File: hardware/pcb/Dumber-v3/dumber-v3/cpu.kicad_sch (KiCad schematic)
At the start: 30 parts, among them J1 Conn_02x03_Odd_Even, J2 Conn_02x03_Odd_Even, J3 Conn_02x05_Odd_Even, M1 Motor, M2 Motor, Q2 PMN52XP, U1 XBEE-3, U2 STM32F071CBTx, U7 A3909

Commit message: Mise a jour PCB et coque. Des fichiers STEP ne sont pas encore remontés car trop gros
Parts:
- removed D3, D4, D5: LED, Diode_SMD:D_0805_2012Metric, symbol Device:LED
- removed R16, R22: 1K, Resistor_SMD:R_0805_2012Metric, symbol Device:R
- removed R23: 820, Resistor_SMD:R_0805_2012Metric, symbol Device:R
- added J4: TE 1-84982-0, INSA:TE 1-84982-0, symbol Connector_Generic:Conn_01x10
- added RN1, RN2: 1K, Resistor_SMD:R_Array_Convex_4x1206, symbol Device:R_Pack04
- J3: footprint Connector_PinHeader_1.27mm:PinHeader_2x05_P1.27mm_Vertical_SMD -> Connector_PinHeader_1.27mm:PinHeader_2x05_P1.27mm_Horizontal
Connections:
- net +2V5: now also U2.36 (VDDIO2)
- net GND: now also J4.1 (Pin_1)
- net SEG_D: now reaches U2.29 (PA8)
- net SEG_D: now also RN1.4 (R4.1)
- net SEG_E: now reaches U2.30 (PA9)
- net SEG_E: now also RN2.4 (R4.1)
- net SEG_F: now reaches U2.32 (PA11)
- net SEG_F: now also RN2.3 (R3.1)
- net SEG_G: now reaches U2.33 (PA12)
- net SEG_G: now also RN2.2 (R2.1)
- net SEG_DP: now reaches U2.38 (PA15)
- net SEG_DP: now also RN2.1 (R1.1)
- net LED_ORANGE renamed SEG_B
- net SEG_B: now also RN1.2 (R2.1)
- net LED_ROUGE renamed SEG_A
- net SEG_A: now also RN1.1 (R1.1)
- net LED_VERTE renamed SEG_C
- net SEG_C: now also RN1.3 (R3.1)
- new net: J4.6 (Pin_6), RN2.5 (R4.2)
- new net: J4.7 (Pin_7), RN2.6 (R3.2)
- new net: J4.8 (Pin_8), RN2.7 (R2.2)
- new net: J4.9 (Pin_9), RN2.8 (R1.2)
- new net: J4.5 (Pin_5), RN1.5 (R4.2)
- new net: J4.4 (Pin_4), RN1.6 (R3.2)
- new net: J4.3 (Pin_3), RN1.7 (R2.2)
- new net: J4.2 (Pin_2), RN1.8 (R1.2)
- new net BUTTON_PRESS: J4.10 (Pin_10)
- no-connect marks 16 -> 24

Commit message: Mise a jour sur les pcbs de dumber v3
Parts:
- removed RN1, RN2: 1K, Resistor_SMD:R_Array_Convex_4x1206, symbol Device:R_Pack04
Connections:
- net SEG_A: now also J4.2 (Pin_2)
- net SEG_B: now also J4.3 (Pin_3)
- net SEG_C: now also J4.4 (Pin_4)
- net SEG_D: now also J4.5 (Pin_5)
- net SEG_DP: now also J4.9 (Pin_9)
- net SEG_E: now also J4.6 (Pin_6)
- net SEG_F: now also J4.7 (Pin_7)
- net SEG_G: now also J4.8 (Pin_8)
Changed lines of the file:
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@@
     (stroke (width 0) (type default) (color 0 0 0 0))
   )
-  (wire (pts (xy 39.37 50.8) (xy 39.37 45.72))
+  (wire (pts (xy 39.37 45.72) (xy 39.37 69.85))
     (stroke (width 0) (type default) (color 0 0 0 0))
   )
@@
     (stroke (width 0) (type default) (color 0 0 0 0))
   )
-  (wire (pts (xy 34.29 60.96) (xy 34.29 80.01))
-    (stroke (width 0) (type default) (color 0 0 0 0))
-  )
-  (wire (pts (xy 52.07 50.8) (xy 52.07 45.72))
+  (wire (pts (xy 52.07 45.72) (xy 52.07 69.85))
     (stroke (width 0) (type default) (color 0 0 0 0))
   )
@@
     (stroke (width 0) (type default) (color 0 0 0 0))
   )
-  (wire (pts (xy 36.83 50.8) (xy 36.83 44.45))
+  (wire (pts (xy 36.83 44.45) (xy 36.83 69.85))
     (stroke (width 0) (type default) (color 0 0 0 0))
   )
@@
     (stroke (width 0) (type default) (color 0 0 0 0))
   )
-  (wire (pts (xy 54.61 39.37) (xy 54.61 50.8))
+  (wire (pts (xy 54.61 39.37) (xy 54.61 69.85))
     (stroke (width 0) (type default) (color 0 0 0 0))
   )
@@
     (stroke (width 0) (type default) (color 0 0 0 0))
   )
-  (wire (pts (xy 31.75 60.96) (xy 31.75 80.01))
-    (stroke (width 0) (type default) (color 0 0 0 0))
-  )
   (wire (pts (xy 240.03 99.06) (xy 240.03 101.6))
     (stroke (width 0) (type default) (color 0 0 0 0))
@@
     (stroke (width 0) (type default) (color 0 0 0 0))
   )
-  (wire (pts (xy 54.61 60.96) (xy 54.61 80.01))
-    (stroke (width 0) (type default) (color 0 0 0 0))
-  )
   (wire (pts (xy 201.93 33.02) (xy 201.93 35.56))
     (stroke (width 0) (type default) (color 0 0 0 0))
   )
-  (wire (pts (xy 59.69 60.96) (xy 59.69 80.01))
-    (stroke (width 0) (type default) (color 0 0 0 0))
-  )
   (wire (pts (xy 232.41 29.21) (xy 232.41 38.1))
     (stroke (width 0) (type default) (color 0 0 0 0))
@@
     (stroke (width 0) (type default) (color 0 0 0 0))
   )
-  (wire (pts (xy 34.29 50.8) (xy 34.29 43.18))
+  (wire (pts (xy 34.29 43.18) (xy 34.29 69.85))
     (stroke (width 0) (type default) (color 0 0 0 0))
   )
@@
     (stroke (width 0) (type default) (color 0 0 0 0))
   )
-  (wire (pts (xy 57.15 50.8) (xy 57.15 41.91))
+  (wire (pts (xy 57.15 41.91) (xy 57.15 69.85))
     (stroke (width 0) (type default) (color 0 0 0 0))
   )
@@
     (stroke (width 0) (type default) (color 0 0 0 0))
   )
-  (wire (pts (xy 31.75 50.8) (xy 31.75 41.91))
-    (stroke (width 0) (type default) (color 0 0 0 0))
-  )
-  (wire (pts (xy 57.15 60.96) (xy 57.15 80.01))
+  (wire (pts (xy 31.75 41.91) (xy 31.75 69.85))
     (stroke (width 0) (type default) (color 0 0 0 0))
   )
@@
     (stroke (width 0) (type default) (color 0 0 0 0))
   )
-  (wire (pts (xy 59.69 50.8) (xy 59.69 43.18))
+  (wire (pts (xy 59.69 43.18) (xy 59.69 69.85))
     (stroke (width 0) (type default) (color 0 0 0 0))
   )
@@
     (stroke (width 0) (type default) (color 0 0 0 0))
   )
-  (wire (pts (xy 52.07 60.96) (xy 52.07 80.01))
-    (stroke (width 0) (type default) (color 0 0 0 0))
-  )
   (wire (pts (xy 110.49 78.74) (xy 116.84 78.74))
     (stroke (width 0) (type default) (color 0 0 0 0))
@@
     (stroke (width 0) (type default) (color 0 0 0 0))
   )
-  (wire (pts (xy 36.83 60.96) (xy 36.83 80.01))
-    (stroke (width 0) (type default) (color 0 0 0 0))
-  )
   (wire (pts (xy 113.03 48.26) (xy 116.84 48.26))
     (stroke (width 0) (type default) (color 0 0 0 0))
@@
     (stroke (width 0) (type default) (color 0 0 0 0))
   )
-  (wire (pts (xy 39.37 60.96) (xy 39.37 80.01))
-    (stroke (width 0) (type default) (color 0 0 0 0))
-  )
   (label "ENCDROIT_B" (at 172.72 78.74 180)
     (effects (font (size 1.27 1.27)) (justify right bottom))
@@
     (effects (font (size 1.27 1.27)) (justify right bottom))
   )
-  (label "SEG_F" (at 57.15 80.01 90)
-    (effects (font (size 1.27 1.27)) (justify left bottom))
-  )
-  (label "SEG_A" (at 31.75 80.01 90)
+  (label "SEG_F" (at 57.15 69.85 90)
+    (effects (font (size 1.27 1.27)) (justify left bottom))
+  )
+  (label "SEG_A" (at 31.75 69.85 90)
     (effects (font (size 1.27 1.27)) (justify left bottom))
   )
@@
     (effects (font (size 1.27 1.27)) (justify right bottom))
   )
-  (label "SEG_G" (at 54.61 80.01 90)
+  (label "SEG_G" (at 54.61 69.85 90)
     (effects (font (size 1.27 1.27)) (justify left bottom))
   )
@@
     (effects (font (size 1.27 1.27)) (justify right bottom))
   )
-  (label "SEG_C" (at 36.83 80.01 90)
-    (effects (font (size 1.27 1.27)) (justify left bottom))
-  )
-  (label "SEG_DP" (at 52.07 80.01 90)
+  (label "SEG_C" (at 36.83 69.85 90)
+    (effects (font (size 1.27 1.27)) (justify left bottom))
+  )
+  (label "SEG_DP" (at 52.07 69.85 90)
     (effects (font (size 1.27 1.27)) (justify left bottom))
   )
@@
     (effects (font (size 1.27 1.27)) (justify right bottom))
   )
-  (label "SEG_E" (at 59.69 80.01 90)
+  (label "SEG_E" (at 59.69 69.85 90)
     (effects (font (size 1.27 1.27)) (justify left bottom))
   )
@@
     (effects (font (size 1.27 1.27)) (justify right bottom))
   )
-  (label "SEG_B" (at 34.29 80.01 90)
+  (label "SEG_B" (at 34.29 69.85 90)
     (effects (font (size 1.27 1.27)) (justify left bottom))
   )
@@
     (effects (font (size 1.27 1.27)) (justify right bottom))
   )
-  (label "SEG_D" (at 39.37 80.01 90)
+  (label "SEG_D" (at 39.37 69.85 90)
     (effects (font (size 1.27 1.27)) (justify left bottom))
   )
@@
     (pin "1")
   )
-  (symbol (lib_id "Device:R_Pack04") (at 57.15 55.88 0) (unit 1)
-    (in_bom yes) (on_board yes) (fields_autoplaced)
-    (property "Reference" "RN2" (id 0) (at 61.722 55.0453 0)
-      (effects (font (size 1.27 1.27)) (justify left))
-    )
-    (property "Value" "1K" (id 1) (at 61.722 57.5822 0)
-      (effects (font (size 1.27 1.27)) (justify left))
-    )
-    (property "Footprint" "Resistor_SMD:R_Array_Convex_4x1206" (id 2) (at 64.135 55.88 90)
-      (effects (font (size 1.27 1.27)) hide)
-    )
-    (property "Datasheet" "~" (id 3) (at 57.15 55.88 0)
-      (effects (font (size 1.27 1.27)) hide)
-    )
-    (pin "1")
-    (pin "2")
-    (pin "3")
-    (pin "4")
-    (pin "5")
-    (pin "6")
-    (pin "7")
-    (pin "8")
-  )
   (symbol (lib_id "Device:C") (at 275.59 77.47 0) (unit 1)
     (in_bom yes) (on_board yes) (fields_autoplaced)
@@
     (pin "2")
   )
-  (symbol (lib_id "Device:R_Pack04") (at 36.83 55.88 0) (unit 1)
-    (in_bom yes) (on_board yes) (fields_autoplaced)
-    (property "Reference" "RN1" (id 0) (at 41.402 55.0453 0)
-      (effects (font (size 1.27 1.27)) (justify left))
-    )
-    (property "Value" "1K" (id 1) (at 41.402 57.5822 0)
-      (effects (font (size 1.27 1.27)) (justify left))
-    )
-    (property "Footprint" "Resistor_SMD:R_Array_Convex_4x1206" (id 2) (at 43.815 55.88 90)
-      (effects (font (size 1.27 1.27)) hide)
-    )
-    (property "Datasheet" "~" (id 3) (at 36.83 55.88 0)
-      (effects (font (size 1.27 1.27)) hide)
-    )
-    (pin "1")
-    (pin "2")
-    (pin "3")
-    (pin "4")
-    (pin "5")
-    (pin "6")
-    (pin "7")
-    (pin "8")
-  )
   (symbol (lib_id "power:GND") (at 49.53 175.26 0) (unit 1)

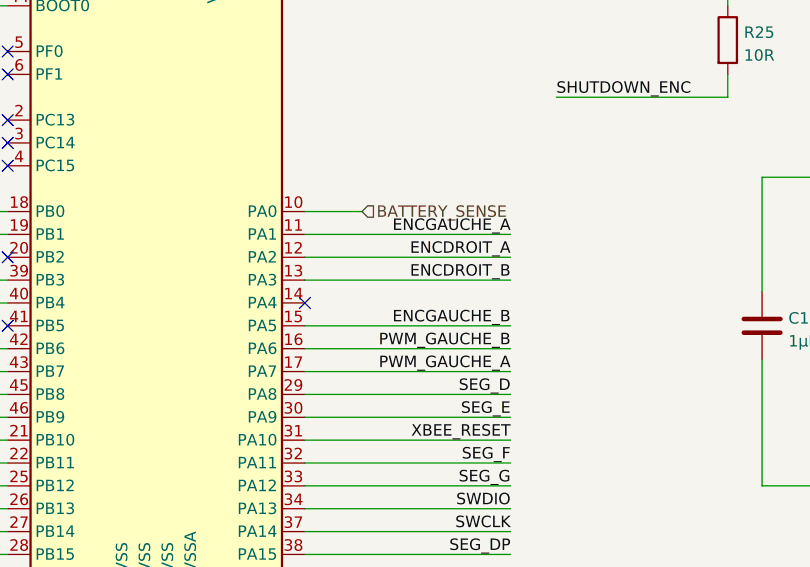
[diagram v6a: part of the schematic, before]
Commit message: asservissement moteur de base OK
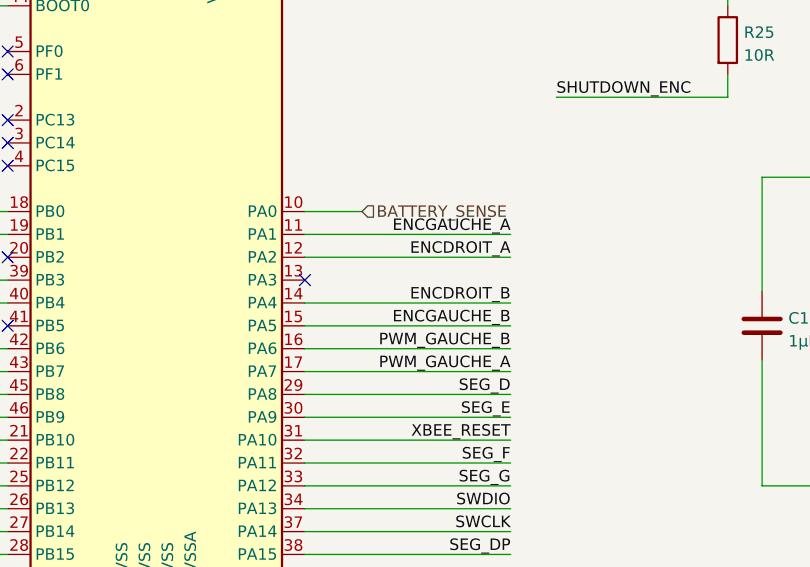
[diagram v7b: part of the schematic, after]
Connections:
- net ENCDROIT_B: now also U2.14 (PA4); no longer U2.13 (PA3)
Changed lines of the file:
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@@
   (title_block
     (title "CPU + Com + Motors")
-    (date "2022-06-08")
-    (rev "1.0")
+    (date "2023-03-29")
+    (rev "2.1")
     (company "INSA - GEI")
   )
@@
   )
   (no_connect (at 116.84 66.04))
-  (no_connect (at 149.86 81.28))
+  (no_connect (at 149.86 78.74))
   (no_connect (at 116.84 83.82))
   (no_connect (at 116.84 76.2))
@@
     (stroke (width 0) (type default) (color 0 0 0 0))
   )
-  (wire (pts (xy 149.86 78.74) (xy 172.72 78.74))
-    (stroke (width 0) (type default) (color 0 0 0 0))
-  )
   (wire (pts (xy 64.77 138.43) (xy 82.55 138.43))
     (stroke (width 0) (type default) (color 0 0 0 0))
@@
     (stroke (width 0) (type default) (color 0 0 0 0))
   )
+  (wire (pts (xy 149.86 81.28) (xy 172.72 81.28))
+    (stroke (width 0) (type default) (color 0 0 0 0))
+  )
   (wire (pts (xy 129.54 33.02) (xy 129.54 38.1))
     (stroke (width 0) (type default) (color 0 0 0 0))
@@
     (stroke (width 0) (type default) (color 0 0 0 0))
   )
-  (label "ENCDROIT_B" (at 172.72 78.74 180)
+  (label "ENCDROIT_B" (at 172.72 81.28 180)
     (effects (font (size 1.27 1.27)) (justify right bottom))
   )
